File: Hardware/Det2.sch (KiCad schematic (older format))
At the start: 45 parts, among them U3 MAX4477, U4 MAX4477, U5 MAX4477

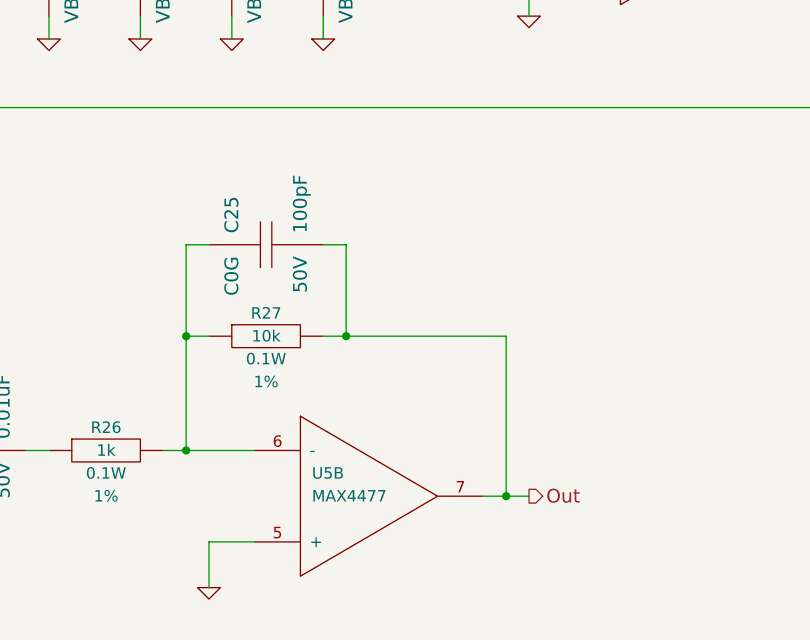
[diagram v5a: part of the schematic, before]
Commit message: New signal chain layout
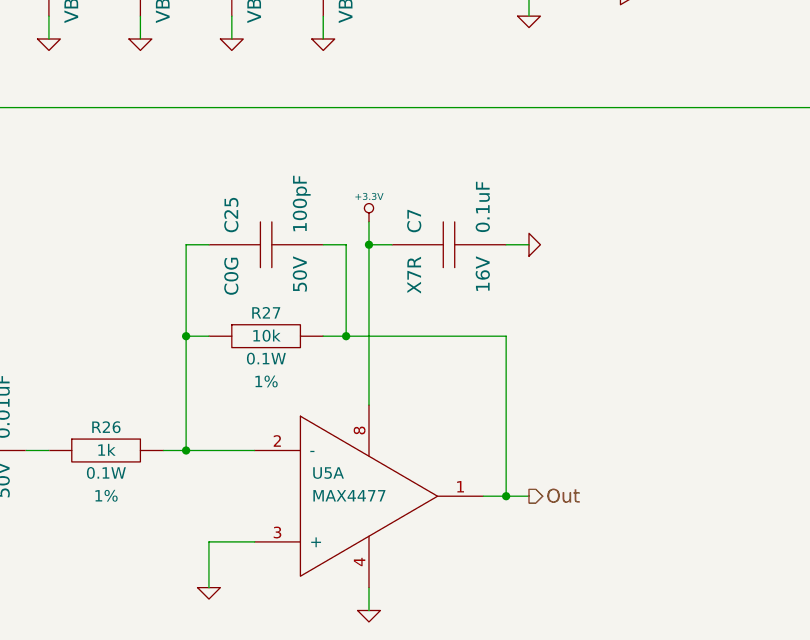
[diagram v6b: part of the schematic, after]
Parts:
- added C7: 0.1uF, CAPC1608, symbol C
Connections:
- net +3.3V: now also U5.8, C7.1
- net GND: now also U5.3 (+), U5.4, C7.2; no longer U5.5 (+)
- net Out: now also U5.1; no longer U5.7
- net at C25.1, R26.2, R27.1: now also U5.2 (-); no longer U5.6 (-)
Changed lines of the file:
@@
 Sheet 4 5
 Title "Solid State Cosmic Ray Detector"
-Date "24 dec 2013"
+Date "26 dec 2013"
 Rev "1"
 Comp "Ethan Harstad"
@@
 $EndDescr
 $Comp
-L GND #PWR053
+L GND #PWR051
 U 1 1 52B956C3
 P 1800 2600
-F 0 "#PWR053" H 1800 2600 30  0001 C CNN
+F 0 "#PWR051" H 1800 2600 30  0001 C CNN
 F 1 "GND" H 1800 2530 30  0001 C CNN
 F 2 "" H 1800 2600 60  0000 C CNN
@@
 $EndComp
 $Comp
-L GND #PWR054
+L GND #PWR052
 U 1 1 52B956C9
 P 2200 2600
-F 0 "#PWR054" H 2200 2600 30  0001 C CNN
+F 0 "#PWR052" H 2200 2600 30  0001 C CNN
 F 1 "GND" H 2200 2530 30  0001 C CNN
 F 2 "" H 2200 2600 60  0000 C CNN
@@
 $EndComp
 $Comp
-L GND #PWR055
+L GND #PWR053
 U 1 1 52B956CF
 P 3000 2600
-F 0 "#PWR055" H 3000 2600 30  0001 C CNN
+F 0 "#PWR053" H 3000 2600 30  0001 C CNN
 F 1 "GND" H 3000 2530 30  0001 C CNN
 F 2 "" H 3000 2600 60  0000 C CNN
@@
 $EndComp
 $Comp
-L GND #PWR056
+L GND #PWR054
 U 1 1 52B956D5
 P 2600 2600
-F 0 "#PWR056" H 2600 2600 30  0001 C CNN
+F 0 "#PWR054" H 2600 2600 30  0001 C CNN
 F 1 "GND" H 2600 2530 30  0001 C CNN
 F 2 "" H 2600 2600 60  0000 C CNN
@@
 Out
 $Comp
-L +12V #PWR057
+L +12V #PWR055
 U 1 1 52B956DC
 P 900 1200
-F 0 "#PWR057" H 900 1150 20  0001 C CNN
+F 0 "#PWR055" H 900 1150 20  0001 C CNN
 F 1 "+12V" H 900 1300 30  0000 C CNN
 F 2 "" H 900 1200 60  0000 C CNN
@@
 $EndComp
 $Comp
-L GND #PWR058
+L GND #PWR056
 U 1 1 52B956ED
 P 900 5000
-F 0 "#PWR058" H 900 5000 30  0001 C CNN
+F 0 "#PWR056" H 900 5000 30  0001 C CNN
 F 1 "GND" H 900 4930 30  0001 C CNN
 F 2 "" H 900 5000 60  0000 C CNN
@@
 $EndComp
 $Comp
-L GND #PWR059
+L GND #PWR057
 U 1 1 52B956FC
 P 3400 2600
-F 0 "#PWR059" H 3400 2600 30  0001 C CNN
+F 0 "#PWR057" H 3400 2600 30  0001 C CNN
 F 1 "GND" H 3400 2530 30  0001 C CNN
 F 2 "" H 3400 2600 60  0000 C CNN
@@
 $EndComp
 $Comp
-L GND #PWR060
+L GND #PWR058
 U 1 1 52B95702
 P 3800 2600
-F 0 "#PWR060" H 3800 2600 30  0001 C CNN
+F 0 "#PWR058" H 3800 2600 30  0001 C CNN
 F 1 "GND" H 3800 2530 30  0001 C CNN
 F 2 "" H 3800 2600 60  0000 C CNN
@@
 $EndComp
 $Comp
-L GND #PWR061
+L GND #PWR059
 U 1 1 52B95708
 P 4600 2600
-F 0 "#PWR061" H 4600 2600 30  0001 C CNN
+F 0 "#PWR059" H 4600 2600 30  0001 C CNN
 F 1 "GND" H 4600 2530 30  0001 C CNN
 F 2 "" H 4600 2600 60  0000 C CNN
@@
 $EndComp
 $Comp
-L GND #PWR062
+L GND #PWR060
 U 1 1 52B9570E
 P 4200 2600
-F 0 "#PWR062" H 4200 2600 30  0001 C CNN
+F 0 "#PWR060" H 4200 2600 30  0001 C CNN
 F 1 "GND" H 4200 2530 30  0001 C CNN
 F 2 "" H 4200 2600 60  0000 C CNN
@@
 $EndComp
 $Comp
-L GND #PWR063
+L GND #PWR061
 U 1 1 52B95769
 P 1800 5000
-F 0 "#PWR063" H 1800 5000 30  0001 C CNN
+F 0 "#PWR061" H 1800 5000 30  0001 C CNN
 F 1 "GND" H 1800 4930 30  0001 C CNN
 F 2 "" H 1800 5000 60  0000 C CNN
@@
 $EndComp
 $Comp
-L GND #PWR064
+L GND #PWR062
 U 1 1 52B9576F
 P 2200 5000
-F 0 "#PWR064" H 2200 5000 30  0001 C CNN
+F 0 "#PWR062" H 2200 5000 30  0001 C CNN
 F 1 "GND" H 2200 4930 30  0001 C CNN
 F 2 "" H 2200 5000 60  0000 C CNN
@@
 $EndComp
 $Comp
-L GND #PWR065
+L GND #PWR063
 U 1 1 52B95775
 P 3000 5000
-F 0 "#PWR065" H 3000 5000 30  0001 C CNN
+F 0 "#PWR063" H 3000 5000 30  0001 C CNN
 F 1 "GND" H 3000 4930 30  0001 C CNN
 F 2 "" H 3000 5000 60  0000 C CNN
@@
 $EndComp
 $Comp
-L GND #PWR066
+L GND #PWR064
 U 1 1 52B9577B
 P 2600 5000
-F 0 "#PWR066" H 2600 5000 30  0001 C CNN
+F 0 "#PWR064" H 2600 5000 30  0001 C CNN
 F 1 "GND" H 2600 4930 30  0001 C CNN
 F 2 "" H 2600 5000 60  0000 C CNN
@@
 $EndComp
 $Comp
-L GND #PWR067
+L GND #PWR065
 U 1 1 52B9578A
 P 3400 5000
-F 0 "#PWR067" H 3400 5000 30  0001 C CNN
+F 0 "#PWR065" H 3400 5000 30  0001 C CNN
 F 1 "GND" H 3400 4930 30  0001 C CNN
 F 2 "" H 3400 5000 60  0000 C CNN
@@
 $EndComp
 $Comp
-L GND #PWR068
+L GND #PWR066
 U 1 1 52B95790
 P 3800 5000
-F 0 "#PWR068" H 3800 5000 30  0001 C CNN
+F 0 "#PWR066" H 3800 5000 30  0001 C CNN
 F 1 "GND" H 3800 4930 30  0001 C CNN
 F 2 "" H 3800 5000 60  0000 C CNN
@@
 $EndComp
 $Comp
-L GND #PWR069
+L GND #PWR067
 U 1 1 52B95796
 P 4600 5000
-F 0 "#PWR069" H 4600 5000 30  0001 C CNN
+F 0 "#PWR067" H 4600 5000 30  0001 C CNN
 F 1 "GND" H 4600 4930 30  0001 C CNN
 F 2 "" H 4600 5000 60  0000 C CNN
@@
 $EndComp
 $Comp
-L GND #PWR070
+L GND #PWR068
 U 1 1 52B9579C
 P 4200 5000
-F 0 "#PWR070" H 4200 5000 30  0001 C CNN
+F 0 "#PWR068" H 4200 5000 30  0001 C CNN
 F 1 "GND" H 4200 4930 30  0001 C CNN
 F 2 "" H 4200 5000 60  0000 C CNN
@@
 $EndComp
 $Comp
-L GND #PWR071
+L GND #PWR069
 U 1 1 52B9580B
 P 6900 1000
-F 0 "#PWR071" H 6900 1000 30  0001 C CNN
+F 0 "#PWR069" H 6900 1000 30  0001 C CNN
 F 1 "GND" H 6900 930 30  0001 C CNN
 F 2 "" H 6900 1000 60  0000 C CNN
@@
 $EndComp
 $Comp
-L +3.3V #PWR072
+L +3.3V #PWR070
 U 1 1 52B9581C
 P 6200 900
-F 0 "#PWR072" H 6200 860 30  0001 C CNN
+F 0 "#PWR070" H 6200 860 30  0001 C CNN
 F 1 "+3.3V" H 6200 1010 30  0000 C CNN
 F 2 "" H 6200 900 60  0000 C CNN
@@
 Connection ~ 6100 3800
 $Comp
-L GND #PWR073
+L GND #PWR071
 U 1 1 52B958B4
 P 6200 2600
-F 0 "#PWR073" H 6200 2600 30  0001 C CNN
+F 0 "#PWR071" H 6200 2600 30  0001 C CNN
 F 1 "GND" H 6200 2530 30  0001 C CNN
 F 2 "" H 6200 2600 60  0000 C CNN
@@
 	6200 2600 6200 2500
 $Comp
-L GND #PWR074
+L GND #PWR072
 U 1 1 52B958BB
 P 5500 2500
-F 0 "#PWR074" H 5500 2500 30  0001 C CNN
+F 0 "#PWR072" H 5500 2500 30  0001 C CNN
 F 1 "GND" H 5500 2430 30  0001 C CNN
 F 2 "" H 5500 2500 60  0000 C CNN
@@
 	5500 2300 5700 2300
 $Comp
-L GND #PWR075
+L GND #PWR073
 U 1 1 52B958C3
 P 5500 4900
-F 0 "#PWR075" H 5500 4900 30  0001 C CNN
+F 0 "#PWR073" H 5500 4900 30  0001 C CNN
 F 1 "GND" H 5500 4830 30  0001 C CNN
 F 2 "" H 5500 4900 60  0000 C CNN
@@
 $EndComp
 $Comp
-L GND #PWR076
+L GND #PWR074
 U 1 1 52B958E2
 P 1400 7200
-F 0 "#PWR076" H 1400 7200 30  0001 C CNN
+F 0 "#PWR074" H 1400 7200 30  0001 C CNN
 F 1 "GND" H 1400 7130 30  0001 C CNN
 F 2 "" H 1400 7200 60  0000 C CNN
@@
 Connection ~ 8700 2800
 $Comp
-L GND #PWR077
+L GND #PWR075
 U 1 1 52B95946
 P 9500 2400
-F 0 "#PWR077" H 9500 2400 30  0001 C CNN
+F 0 "#PWR075" H 9500 2400 30  0001 C CNN
 F 1 "GND" H 9500 2330 30  0001 C CNN
 F 2 "" H 9500 2400 60  0000 C CNN
@@
 	10000 3500 10200 3500
 $Comp
-L GND #PWR078
+L GND #PWR076
 U 1 1 52B95953
 P 8800 4000
-F 0 "#PWR078" H 8800 4000 30  0001 C CNN
+F 0 "#PWR076" H 8800 4000 30  0001 C CNN
 F 1 "GND" H 8800 3930 30  0001 C CNN
 F 2 "" H 8800 4000 60  0000 C CNN
@@
 $EndComp
 $Comp
-L GND #PWR079
+L GND #PWR077
 U 1 1 52B95959
 P 8100 3900
-F 0 "#PWR079" H 8100 3900 30  0001 C CNN
+F 0 "#PWR077" H 8100 3900 30  0001 C CNN
 F 1 "GND" H 8100 3830 30  0001 C CNN
 F 2 "" H 8100 3900 60  0000 C CNN
@@
 $EndComp
 $Comp
-L +3.3V #PWR080
+L +3.3V #PWR078
 U 1 1 52B95997
 P 8800 2300
-F 0 "#PWR080" H 8800 2260 30  0001 C CNN
+F 0 "#PWR078" H 8800 2260 30  0001 C CNN
 F 1 "+3.3V" H 8800 2410 30  0000 C CNN
 F 2 "" H 8800 2300 60  0000 C CNN
@@
 Connection ~ 5400 7000
 $Comp
-L GND #PWR081
+L GND #PWR079
 U 1 1 52B959CF
 P 4100 7400
-F 0 "#PWR081" H 4100 7400 30  0001 C CNN
+F 0 "#PWR079" H 4100 7400 30  0001 C CNN
 F 1 "GND" H 4100 7330 30  0001 C CNN
 F 2 "" H 4100 7400 60  0000 C CNN
@@
 $Comp
 L OPAMP-DUAL U5
-U 2 1 52B959DB
+U 1 1 52B959DB
 P 4800 7000
 F 0 "U5" H 4550 7100 50  0000 L CNN
@@
 F 5 "MAX4477AUA+" H 4800 7000 60  0001 C CNN "MFR Part No"
 F 6 "MAX4477AUA+-ND" H 4800 7000 60  0001 C CNN "Distributor Part No"
-	2    4800 7000
+	1    4800 7000
 	1    0    0    -1
 $EndComp
@@
 Text Label 4600 4200 1    60   ~ 0
 Det2B
+$Comp
+L GND #PWR080
+U 1 1 52BB5C7D
+P 5500 5900
+F 0 "#PWR080" H 5500 5900 30  0001 C CNN
+F 1 "GND" H 5500 5830 30  0001 C CNN
+F 2 "" H 5500 5900 60  0000 C CNN
+F 3 "" H 5500 5900 60  0000 C CNN
+	1    5500 5900
+	0    -1   -1   0
+$EndComp
+Wire Wire Line
+	5500 5900 5400 5900
+Wire Wire Line
+	4800 5800 4800 6600
+Wire Wire Line
+	4900 5900 4800 5900
+Connection ~ 4800 5900
+$Comp
+L C C7
+U 1 1 52BB5C8C
+P 5150 5900
+F 0 "C7" H 5200 6050 60  0000 L CNN
+F 1 "0.1uF" H 5200 5750 60  0000 L CNN
+F 2 "CAPC1608" H 5150 5900 60  0001 C CNN
+F 3 "~" H 5150 5900 60  0000 C CNN
+F 4 "Samsung" H 5150 5900 60  0001 C CNN "MFR Name"
+F 5 "CL10B104KO8NNNC" H 5150 5900 60  0001 C CNN "MFR Part No"
+F 6 "1276-1005-1-ND" H 5150 5900 60  0001 C CNN "Distributor Part No"
+F 7 "16V" H 5100 5750 60  0000 R CNN "Voltage"
+F 8 "X7R" H 5100 6050 60  0000 R CNN "Dielectric"
+	1    5150 5900
+	0    -1   -1   0
+$EndComp
+$Comp
+L +3.3V #PWR081
+U 1 1 52BB5C92
+P 4800 5800
+F 0 "#PWR081" H 4800 5760 30  0001 C CNN
+F 1 "+3.3V" H 4800 5910 30  0000 C CNN
+F 2 "" H 4800 5800 60  0000 C CNN
+F 3 "" H 4800 5800 60  0000 C CNN
+	1    4800 5800
+	1    0    0    -1
+$EndComp
+$Comp
+L GND #PWR082
+U 1 1 52BB5CBC
+P 4800 7500
+F 0 "#PWR082" H 4800 7500 30  0001 C CNN
+F 1 "GND" H 4800 7430 30  0001 C CNN
+F 2 "" H 4800 7500 60  0000 C CNN
+F 3 "" H 4800 7500 60  0000 C CNN
+	1    4800 7500
+	1    0    0    -1
+$EndComp
+Wire Wire Line
+	4800 7500 4800 7400
 $EndSCHEMATC

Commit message: Additional layout
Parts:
- added C46: 0.1uF, CAPC1608, symbol C
- added R20: 1M, RESC1608, symbol R
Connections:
- net +12V: now also R20.2
- net GND: now also C46.2
- net at C22.1, R22.1, R24.1: no longer R40.1
- new net: C46.1, R20.1, R40.1
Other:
- moved on the sheet: C22, R40
